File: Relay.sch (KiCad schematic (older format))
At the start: 11 parts

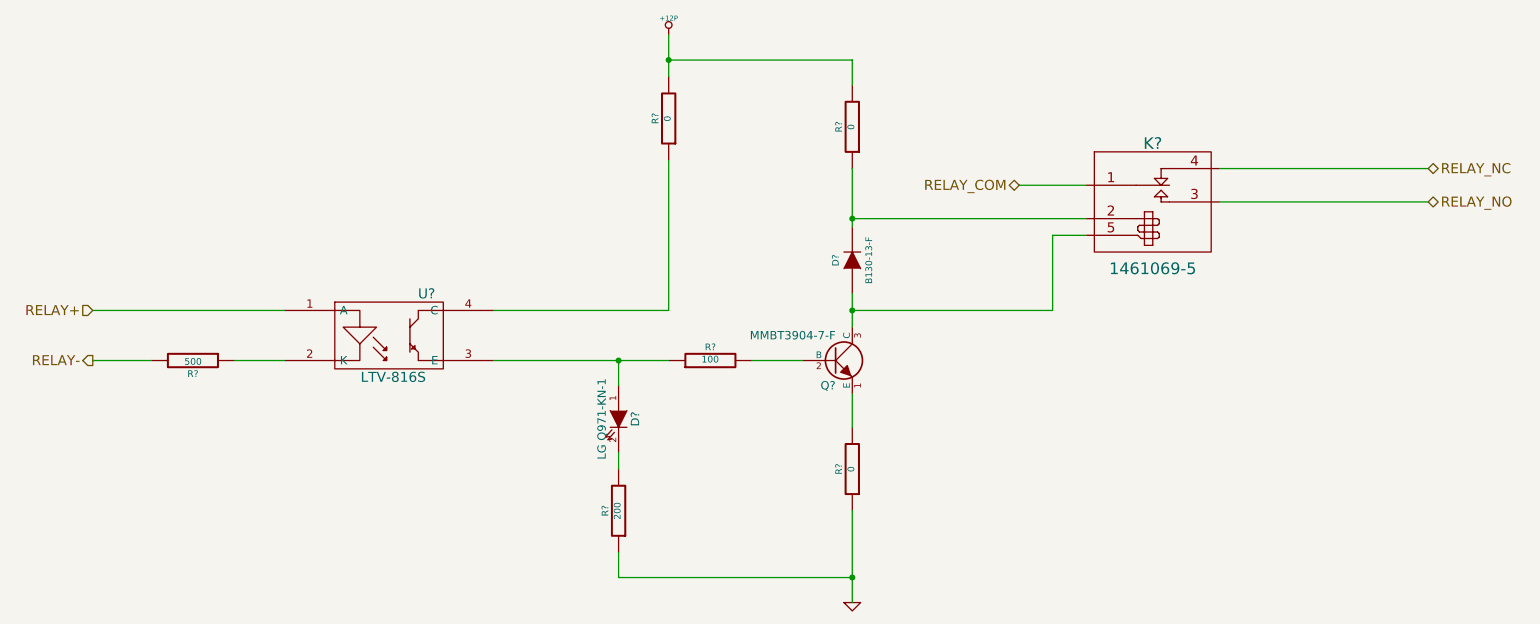
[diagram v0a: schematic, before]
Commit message: Added Arduino Connect Pin Layout
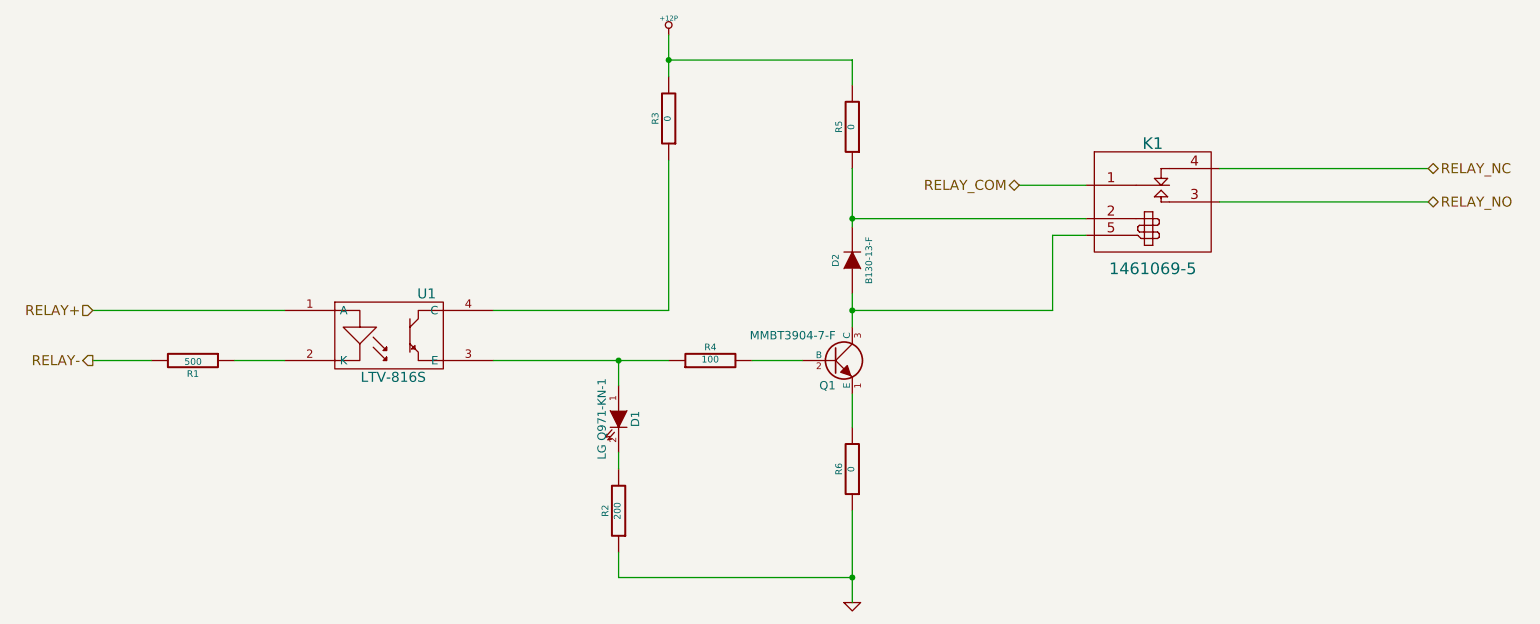
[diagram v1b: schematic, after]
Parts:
- gave numbers to parts that had none: 11
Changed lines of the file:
@@
 RELAY_NO
 $Comp
-L LED D?
+L LED D1
 U 1 1 52F1ADBD
 P 5450 4150
-F 0 "D?" H 5450 4250 50  0000 C CNN
+F 0 "D1" H 5450 4250 50  0000 C CNN
 F 1 "LG Q971-KN-1" H 5450 4050 50  0000 C CNN
 F 2 "~" H 5450 4150 60  0000 C CNN
@@
 $EndComp
 $Comp
-L NPN Q?
+L NPN Q1
 U 1 1 52F1ADCC
 P 6750 3800
-F 0 "Q?" H 6750 3650 50  0000 R CNN
+F 0 "Q1" H 6750 3650 50  0000 R CNN
 F 1 "MMBT3904-7-F" H 6750 3950 50  0000 R CNN
 F 2 "~" H 6750 3800 60  0000 C CNN
@@
 $EndComp
 $Comp
-L SPDT K?
+L SPDT K1
 U 1 1 52F1B21B
 P 8650 2700
-F 0 "K?" H 8650 2900 70  0000 C CNN
+F 0 "K1" H 8650 2900 70  0000 C CNN
 F 1 "1461069-5" H 8650 2150 70  0000 C CNN
 F 2 "~" H 8650 2700 60  0000 C CNN
@@
 RELAY_COM
 $Comp
-L R R?
+L R R4
 U 1 1 52F1B259
 P 6000 3800
-F 0 "R?" V 6080 3800 40  0000 C CNN
+F 0 "R4" V 6080 3800 40  0000 C CNN
 F 1 "100" V 6007 3801 40  0000 C CNN
 F 2 "~" V 5930 3800 30  0000 C CNN
@@
 $EndComp
 $Comp
-L R R?
+L R R6
 U 1 1 52F1B290
 P 6850 4450
-F 0 "R?" V 6930 4450 40  0000 C CNN
+F 0 "R6" V 6930 4450 40  0000 C CNN
 F 1 "0" V 6857 4451 40  0000 C CNN
 F 2 "~" V 6780 4450 30  0000 C CNN
@@
 $EndComp
 $Comp
-L GND #PWR?
+L GND #PWR58
 U 1 1 52F1B29F
 P 6850 5250
-F 0 "#PWR?" H 6850 5250 30  0001 C CNN
+F 0 "#PWR58" H 6850 5250 30  0001 C CNN
 F 1 "GND" H 6850 5180 30  0001 C CNN
 F 2 "" H 6850 5250 60  0000 C CNN
@@
 $EndComp
 $Comp
-L R R?
+L R R2
 U 1 1 52F1B2C7
 P 5450 4700
-F 0 "R?" V 5530 4700 40  0000 C CNN
+F 0 "R2" V 5530 4700 40  0000 C CNN
 F 1 "200" V 5457 4701 40  0000 C CNN
 F 2 "~" V 5380 4700 30  0000 C CNN
@@
 $EndComp
 $Comp
-L R R?
+L R R3
 U 1 1 52F1B2D8
 P 5750 2350
-F 0 "R?" V 5830 2350 40  0000 C CNN
+F 0 "R3" V 5830 2350 40  0000 C CNN
 F 1 "0" V 5757 2351 40  0000 C CNN
 F 2 "~" V 5680 2350 30  0000 C CNN
@@
 	5750 3500 4700 3500
 $Comp
-L R R?
+L R R1
 U 1 1 52F1B37F
 P 2900 3800
-F 0 "R?" V 2980 3800 40  0000 C CNN
+F 0 "R1" V 2980 3800 40  0000 C CNN
 F 1 "500" V 2907 3801 40  0000 C CNN
 F 2 "~" V 2830 3800 30  0000 C CNN
@@
 	2300 3800 2650 3800
 $Comp
-L DIODE D?
+L DIODE D2
 U 1 1 52F1B3D7
 P 6850 3200
-F 0 "D?" H 6850 3300 40  0000 C CNN
+F 0 "D2" H 6850 3300 40  0000 C CNN
 F 1 "B130-13-F" H 6850 3100 40  0000 C CNN
 F 2 "~" H 6850 3200 60  0000 C CNN
@@
 Connection ~ 6850 3500
 $Comp
-L +12P #PWR?
+L +12P #PWR57
 U 1 1 52F24BA2
 P 5750 1850
-F 0 "#PWR?" H 5750 1820 30  0001 C CNN
+F 0 "#PWR57" H 5750 1820 30  0001 C CNN
 F 1 "+12P" H 5750 1950 30  0000 C CNN
 F 2 "" H 5750 1850 60  0000 C CNN
@@
 $EndComp
 $Comp
-L OPTO-TRANSISTOR4 U?
+L OPTO-TRANSISTOR4 U1
 U 1 1 53021786
 P 4100 3650
-F 0 "U?" H 4300 3900 60  0000 C CNN
+F 0 "U1" H 4300 3900 60  0000 C CNN
 F 1 "LTV-816S" H 4100 3400 60  0000 C CNN
 F 2 "" H 4100 3650 60  0000 C CNN
@@
 $EndComp
 $Comp
-L R R?
+L R R5
 U 1 1 53022263
 P 6850 2400
-F 0 "R?" V 6930 2400 40  0000 C CNN
+F 0 "R5" V 6930 2400 40  0000 C CNN
 F 1 "0" V 6857 2401 40  0000 C CNN
 F 2 "~" V 6780 2400 30  0000 C CNN
